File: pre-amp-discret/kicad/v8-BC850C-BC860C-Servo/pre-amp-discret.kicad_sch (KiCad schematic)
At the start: 68 parts, among them J1 Conn_01x01, J2 Conn_01x01, J3 Conn_01x01, J4 Conn_01x01, J5 Conn_01x01, J6 Conn_01x01, J7 Conn_01x01, J8 Conn_01x01, J9 Conn_01x01, Q1 BC860C, Q10 BC850C, Q11 BC860C, Q12 BC860C, Q13 DZT5401, Q14 DZT5401, Q15 BC860C, Q2 BC850C, Q3 BC860C, Q4 BC860C, Q5 BC850C, Q6 BC850C, Q7 BC860C, Q8 BC850C, Q9 BC850C, U1 OPA188xxDBV

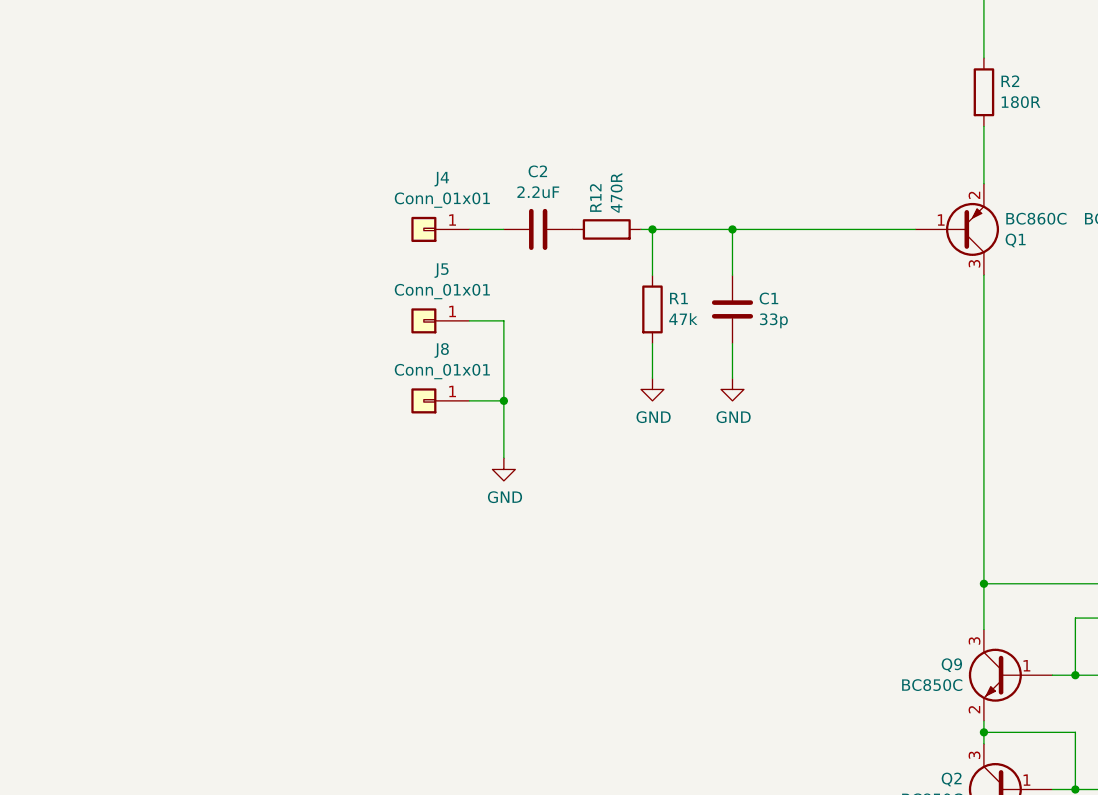
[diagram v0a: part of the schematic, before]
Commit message: update part values and comment
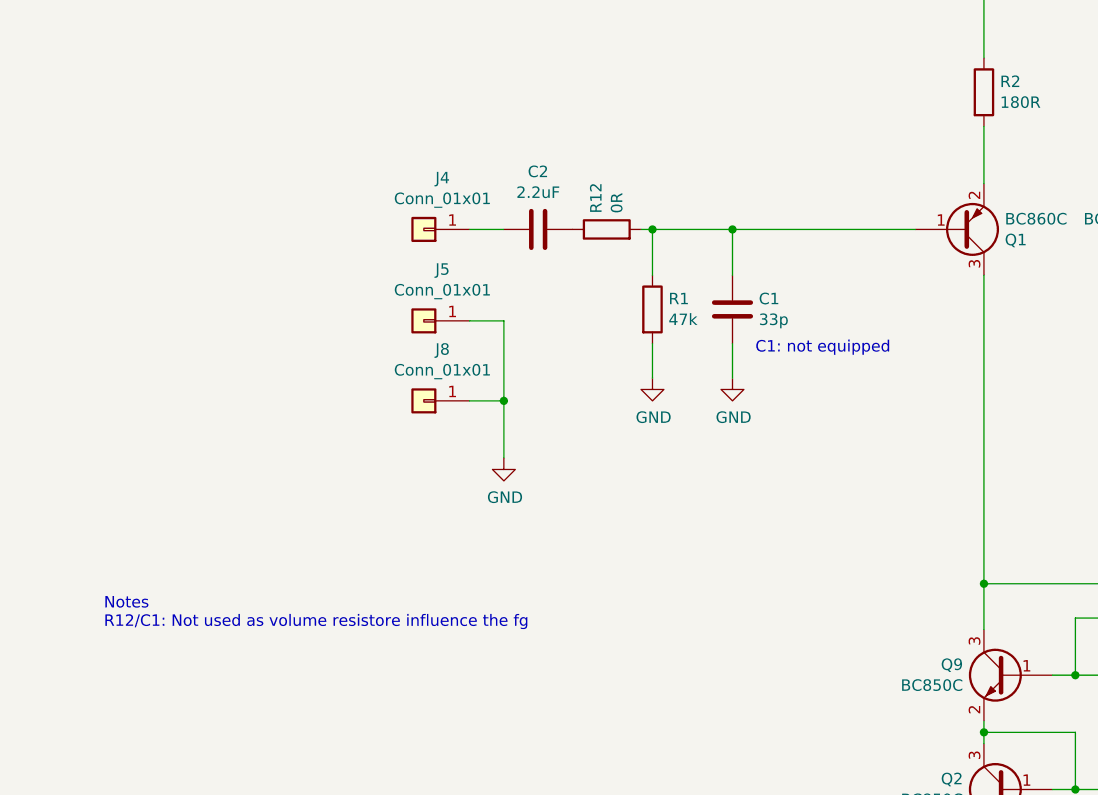
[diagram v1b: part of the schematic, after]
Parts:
- R12: value 470R -> 0R
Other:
- note added: "C1: not equipped"
- note added: "Notes R12/C1: Not used as volume resistore influence the fg"
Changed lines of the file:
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@@
+    (effects (font (size 1.27 1.27)) (justify left bottom))
+  )
+  (text "Notes\nR12/C1: Not used as volume resistore influence the fg"
+    (at 33.02 151.13 0)
     (effects (font (size 1.27 1.27)) (justify left bottom))
   )
@@
     (effects (font (size 1.27 1.27)) (justify left bottom))
   )
+  (text "C1: not equipped" (at 105.41 120.65 0)
+    (effects (font (size 1.27 1.27)) (justify left bottom))
+  )
   (text "7.6mA" (at 217.805 72.39 0)
     (effects (font (size 1.27 1.27)) (justify left bottom))
@@
       (effects (font (size 1.27 1.27)) (justify left))
     )
-    (property "Value" "470R" (id 1) (at 90.043 104.902 0)
+    (property "Value" "0R" (id 1) (at 90.043 104.902 0)
       (effects (font (size 1.27 1.27)) (justify left))
     )
@@
     )
     (path "/1b0cc5f3-21b1-4140-bac3-6f82e778b42b"
-      (reference "R12") (unit 1) (value "470R") (footprint "Resistor_SMD:R_0805_2012Metric_Pad1.20x1.40mm_HandSolder")
+      (reference "R12") (unit 1) (value "0R") (footprint "Resistor_SMD:R_0805_2012Metric_Pad1.20x1.40mm_HandSolder")
     )
     (path "/00000000-0000-0000-0000-00005f87bee5"

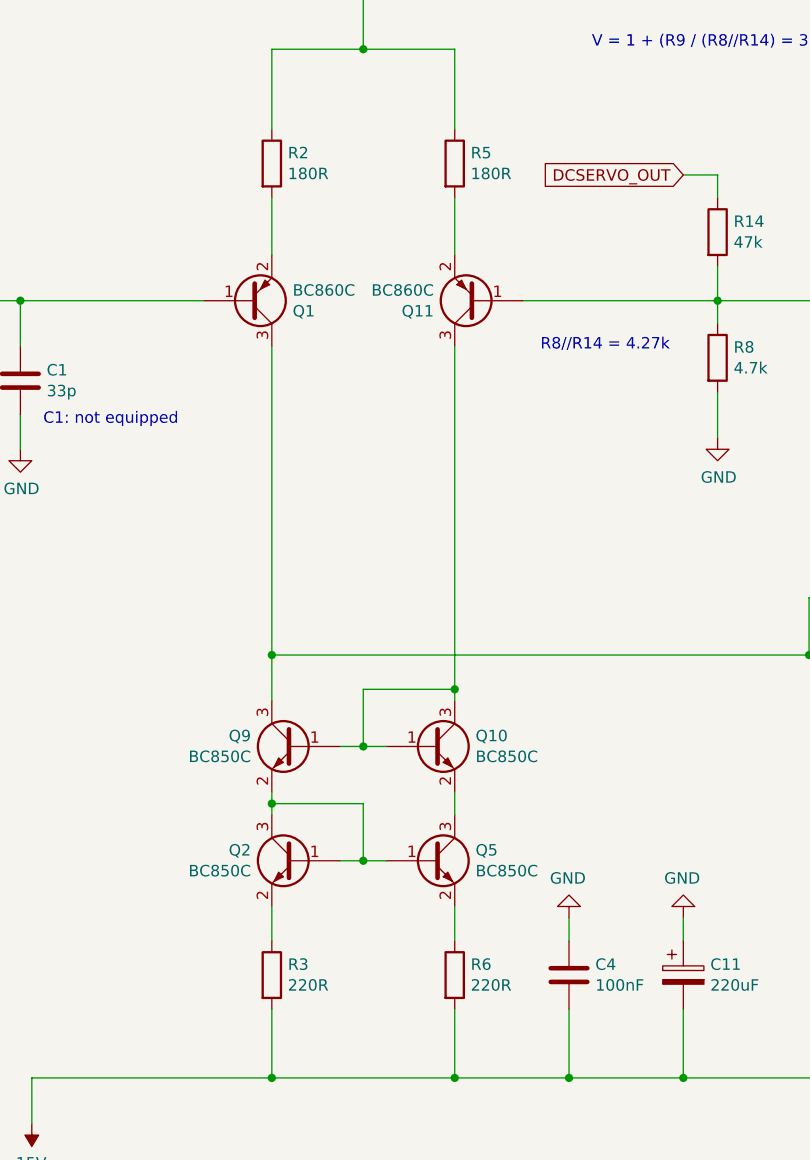
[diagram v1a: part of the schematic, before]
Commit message: Update part values
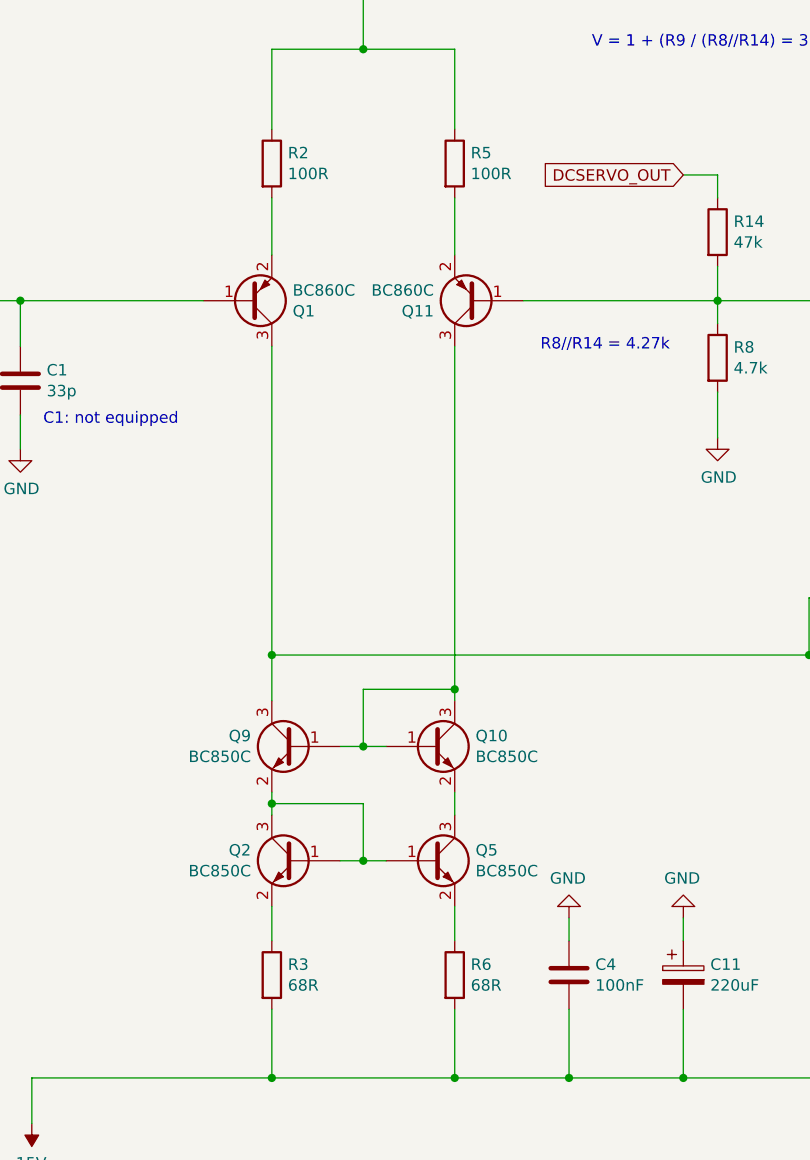
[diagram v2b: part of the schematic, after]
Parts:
- R2, R5: value 180R -> 100R
- R3, R6: value 220R -> 68R
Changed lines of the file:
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@@
   (title_block
     (title "Discrete Pre-Amp")
-    (date "2022-12-29")
+    (date "2023-01-04")
     (rev "V8 BC850C/BC860C")
   )
@@
       (effects (font (size 1.27 1.27)) (justify left))
     )
-    (property "Value" "220R" (id 1) (at 152.908 182.753 0)
+    (property "Value" "68R" (id 1) (at 152.908 182.753 0)
       (effects (font (size 1.27 1.27)) (justify left))
     )
@@
       (effects (font (size 1.27 1.27)) (justify left))
     )
-    (property "Value" "220R" (id 1) (at 132.588 182.753 0)
+    (property "Value" "68R" (id 1) (at 132.588 182.753 0)
       (effects (font (size 1.27 1.27)) (justify left))
     )
@@
       (effects (font (size 1.27 1.27)) (justify left))
     )
-    (property "Value" "180R" (id 1) (at 132.588 92.583 0)
+    (property "Value" "100R" (id 1) (at 132.588 92.583 0)
       (effects (font (size 1.27 1.27)) (justify left))
     )
@@
       (effects (font (size 1.27 1.27)) (justify left))
     )
-    (property "Value" "180R" (id 1) (at 152.908 92.583 0)
+    (property "Value" "100R" (id 1) (at 152.908 92.583 0)
       (effects (font (size 1.27 1.27)) (justify left))
     )
@@
     )
     (path "/00000000-0000-0000-0000-00005f7ffbf9"
-      (reference "R2") (unit 1) (value "180R") (footprint "Resistor_SMD:R_0805_2012Metric_Pad1.20x1.40mm_HandSolder")
+      (reference "R2") (unit 1) (value "100R") (footprint "Resistor_SMD:R_0805_2012Metric_Pad1.20x1.40mm_HandSolder")
     )
     (path "/00000000-0000-0000-0000-00005f7fddc2"
-      (reference "R3") (unit 1) (value "220R") (footprint "Resistor_SMD:R_0805_2012Metric_Pad1.20x1.40mm_HandSolder")
+      (reference "R3") (unit 1) (value "68R") (footprint "Resistor_SMD:R_0805_2012Metric_Pad1.20x1.40mm_HandSolder")
     )
     (path "/00000000-0000-0000-0000-000060b30f20"
@@
     )
     (path "/00000000-0000-0000-0000-00005f800152"
-      (reference "R5") (unit 1) (value "180R") (footprint "Resistor_SMD:R_0805_2012Metric_Pad1.20x1.40mm_HandSolder")
+      (reference "R5") (unit 1) (value "100R") (footprint "Resistor_SMD:R_0805_2012Metric_Pad1.20x1.40mm_HandSolder")
     )
     (path "/00000000-0000-0000-0000-00005f7f7f2c"
-      (reference "R6") (unit 1) (value "220R") (footprint "Resistor_SMD:R_0805_2012Metric_Pad1.20x1.40mm_HandSolder")
+      (reference "R6") (unit 1) (value "68R") (footprint "Resistor_SMD:R_0805_2012Metric_Pad1.20x1.40mm_HandSolder")
     )
     (path "/00000000-0000-0000-0000-000060b30f26"
